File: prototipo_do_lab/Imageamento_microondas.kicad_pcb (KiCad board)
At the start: 2 copper layers, 200 x 150 mm, 89 parts, among them J1 0732511352, J10 0732511352, J11 TB0012-508-03GR, J12 0732511352, J13 0732511352, J2 0732511352, J3 0732511352, J4 0732511352, J5 0732511352, J6 0732511352, J7 0732511352, J8 0732511352, J9 0732511352, U1 SKY13373-460LF, U10 SKY13373-460LF, U11 SKY13373-460LF, U12 SKY13373-460LF, U13 SKY13373-460LF, U14 SKY13373-460LF, U15 SKY13373-460LF, U16 SKY13373-460LF, U17 ESP32-DEVKITC-32E, U18 MCP23016-I_SP, U2 SKY13373-460LF, U3 SKY13373-460LF, U4 SKY13373-460LF, U5 SKY13373-460LF, U6 SKY13373-460LF, U7 SKY13373-460LF, U8 SKY13373-460LF, U9 SKY13373-460LF

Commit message: pin headers added
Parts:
- moved C1 17.3 mm to (128.2, 126.4)
- moved C44 16.3 mm to (178.1, 83.5)
- moved C33 16.3 mm to (172.6, 87.2)
- moved C34 16.3 mm to (176.2, 87.2)
- moved R4 16.3 mm to (172.6, 90.6)
- moved C25 12.1 mm to (101.2, 100.6)
- moved C27 12.1 mm to (95.7, 104.3)
- moved C28 12.1 mm to (99.3, 104.3)
- moved R1 12.1 mm to (95.7, 107.7)
- moved C47 11.1 mm to (210.3, 131.9)
- moved C42 11.1 mm to (208.4, 135.6)
- moved R8 11.1 mm to (204.8, 139.0)
- moved C41 11.1 mm to (204.8, 135.6)
- moved C31 10.9 mm to (66.2, 120.2)
- moved C32 10.9 mm to (69.8, 120.2)
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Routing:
- net /E2_3: track 0.00 -> 84.4 mm
- net (no net): track 84.4 -> 0.00 mm, vias 1 -> 60
- net /CE2_4: vias 0 -> 2
- net /CA_6: vias 0 -> 1
- net /CA_2: vias 0 -> 1

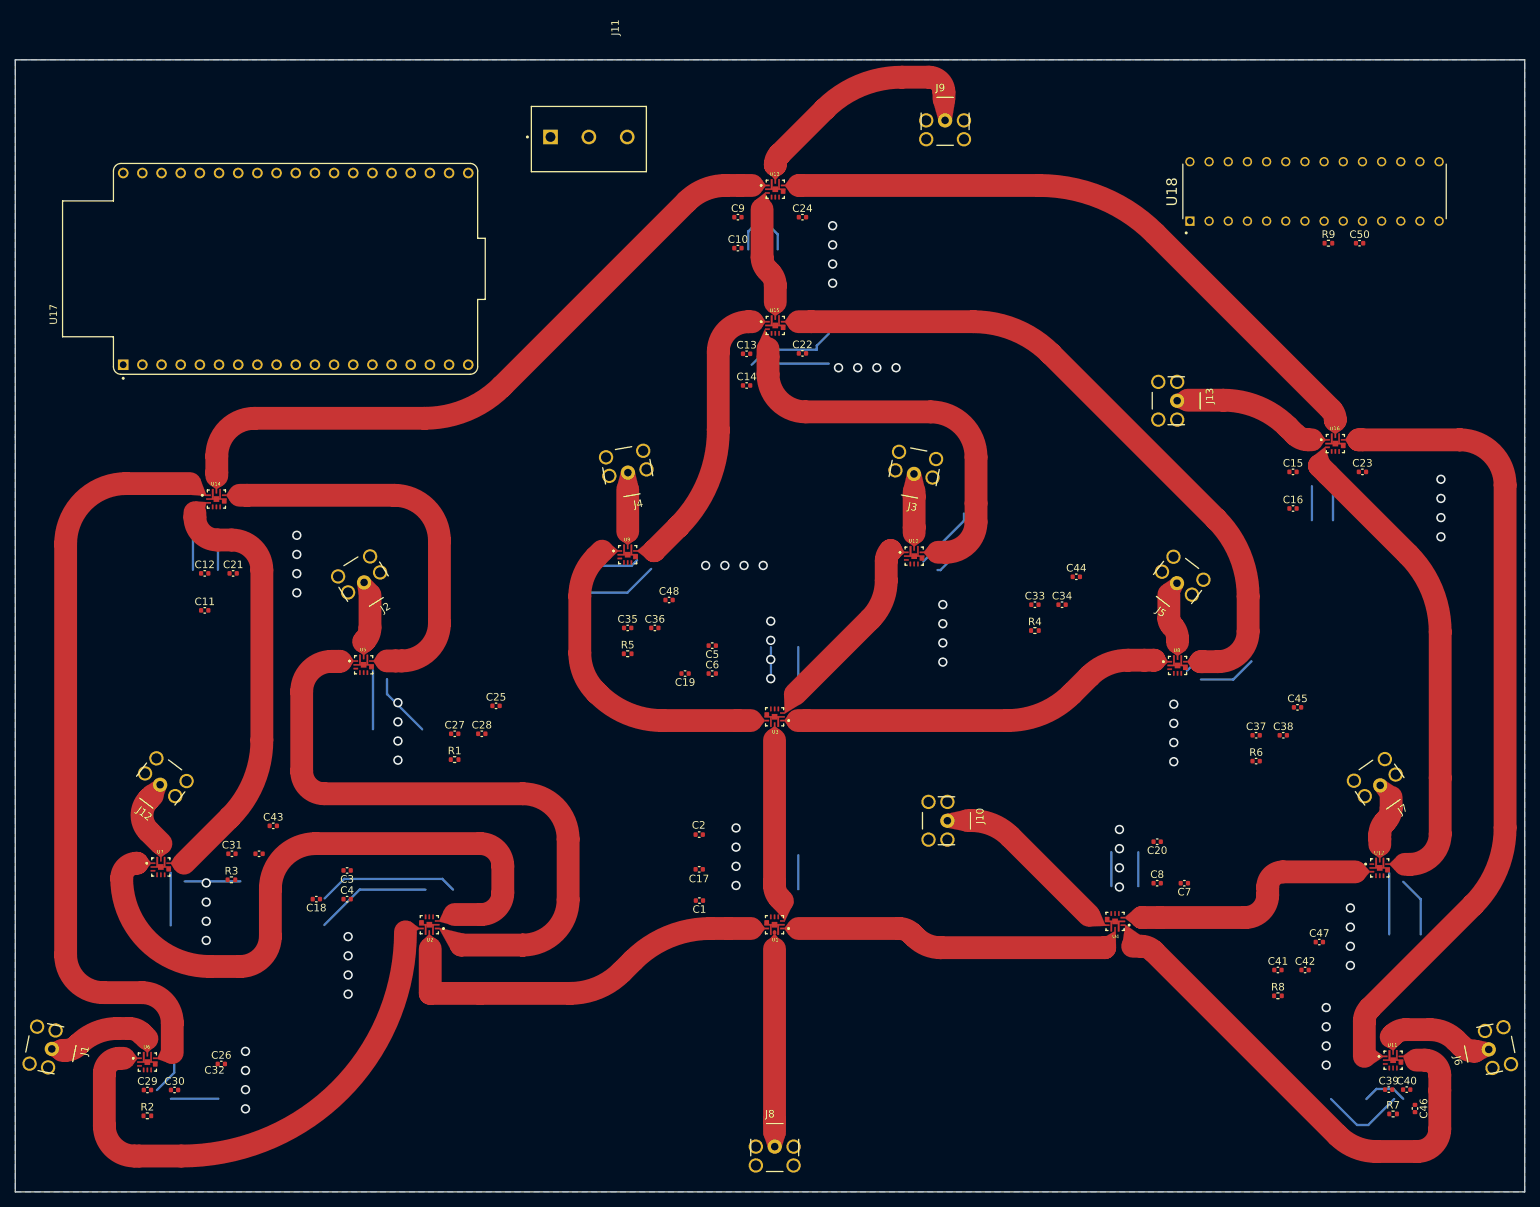
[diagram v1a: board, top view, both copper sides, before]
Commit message: board finished still need validation
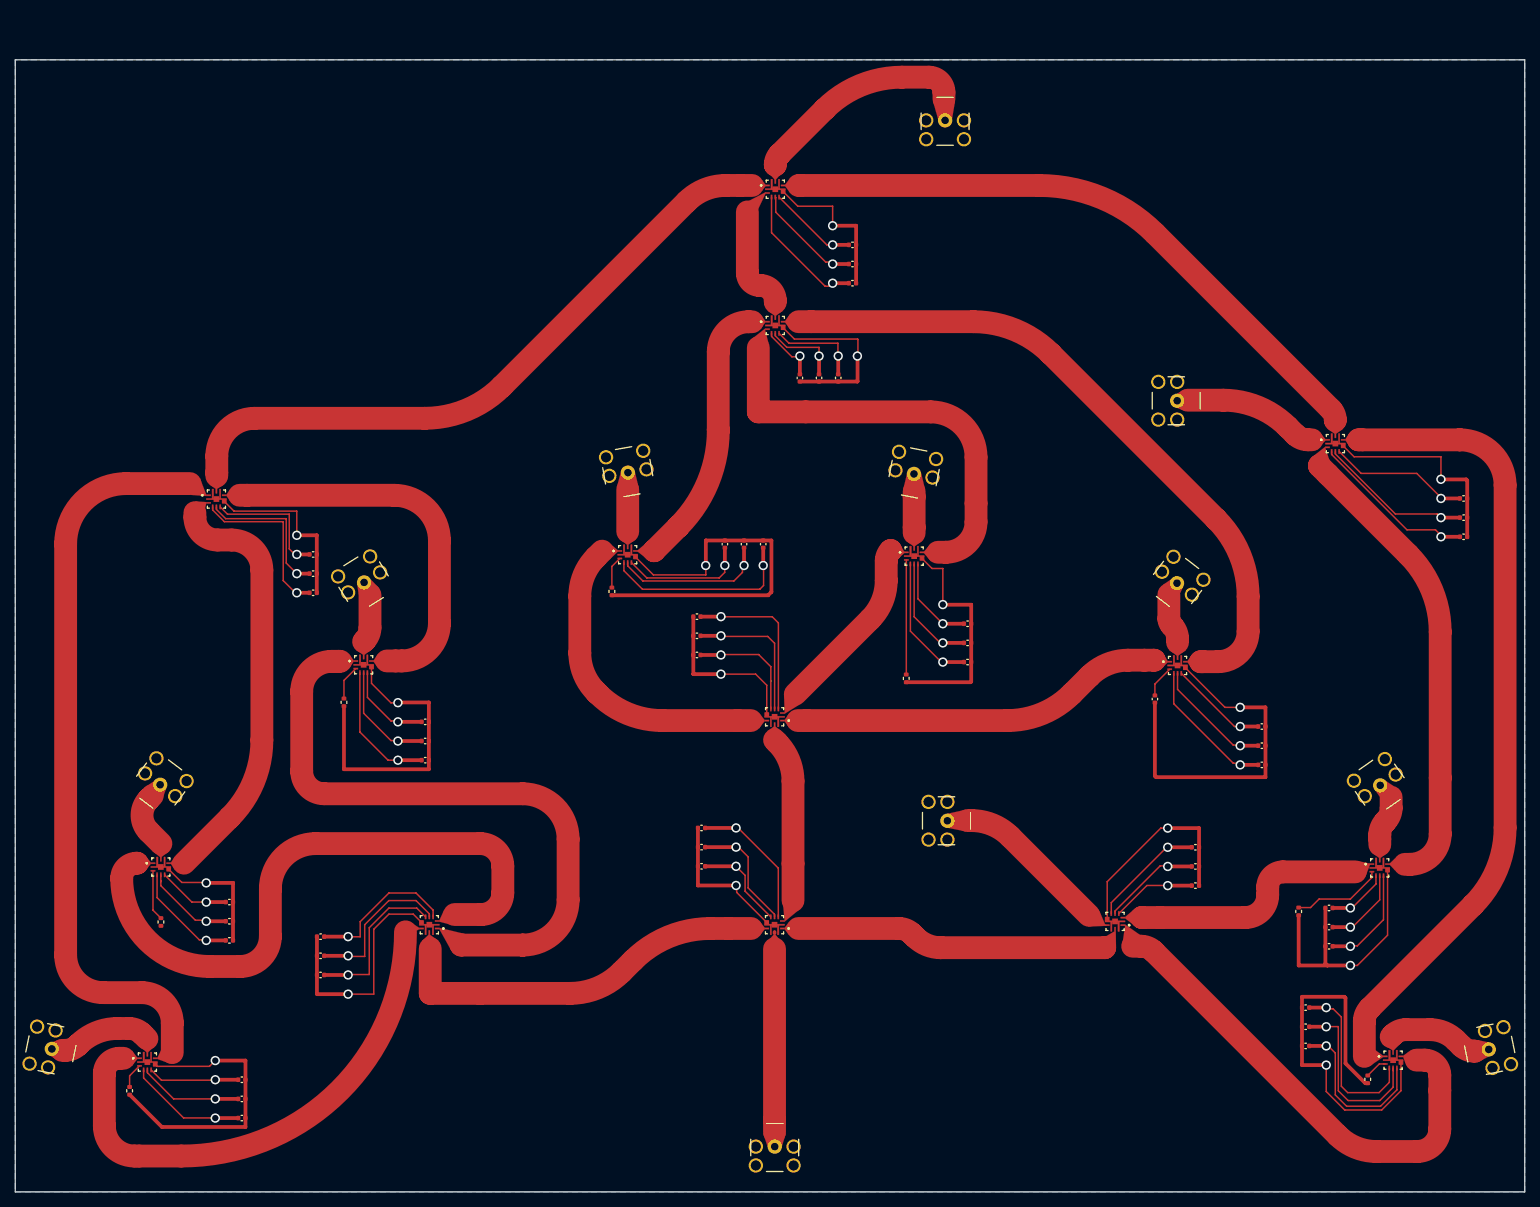
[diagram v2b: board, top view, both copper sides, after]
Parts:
- removed C50: C, Capacitor_SMD:C_0402_1005Metric
- removed J11: TB0012-508-03GR, Conector_alimentacao:SAMESKY_TB0012-508-03GR
- removed R9: R, Resistor_SMD:R_0402_1005Metric
- removed U17: ESP32-DEVKITC-32E, ESP32:MODULE_ESP32-DEVKITC-32E
- removed U18: MCP23016-I_SP, Extensor:DIP787W46P254L3467H508Q28
- moved C15 24.2 mm to (229.4, 78.2), turned to 180 degrees
- moved C16 22.6 mm to (229.4, 75.7)
- moved C35 21.1 mm to (136.6, 79.2), turned to -90 degrees
- moved R4 18.2 mm to (155.6, 97.0), turned to -90 degrees
- moved C9 17.5 mm to (148.4, 44.6), turned to 180 degrees
- moved C46 16.7 mm to (208.5, 145.7), turned to 180 degrees
- moved R1 16.5 mm to (81.0, 100.1), turned to -90 degrees
- moved C36 16.2 mm to (134.1, 79.2), turned to 90 degrees
- moved C40 15.8 mm to (208.5, 143.1), turned to 180 degrees
- moved R6 15.7 mm to (188.5, 99.7), turned to -90 degrees
- moved C44 15.7 mm to (163.7, 89.7)
- moved C39 15.5 mm to (208.5, 140.6)
- moved C10 15.3 mm to (148.4, 42.1)
- moved C11 14.6 mm to (77.0, 85.6), turned to 180 degrees
- moved C12 14.4 mm to (77.0, 83.1)
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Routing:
- net GND: track 0.00 -> 505.4 mm, vias 0 -> 16
- net VDD: track 0.00 -> 236.3 mm, vias 0 -> 16
- net /E2_8: track 0.00 -> 32.0 mm
- net Net-(U12-J3): track 32.0 -> 12.1 mm
- net /CA_9: track 7.85 -> 25.8 mm, vias 0 -> 1
- net /CR2_1: track 4.52 -> 22.4 mm, vias 0 -> 1
- net /CA_14: track 5.99 -> 23.8 mm, vias 0 -> 1
- net /CE2_3: track 4.49 -> 22.1 mm, vias 0 -> 1
- net /CR2_5: track 4.50 -> 22.0 mm, vias 0 -> 1
- net /CR2_6: track 4.70 -> 20.3 mm, vias 0 -> 1
- net Net-(U10-J3): track 0.00 -> 15.2 mm
- net /CR1_1: track 3.03 -> 18.1 mm, vias 0 -> 1
- net /CR2_2: track 4.76 -> 19.6 mm, vias 0 -> 1
- net /CE2_4: track 4.50 -> 18.9 mm, vias 2 -> 1
- net /CE1_1: track 4.50 -> 18.4 mm, vias 0 -> 1
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- added copper zone on B.Cu, net GND
- removed copper zone on B.Cu, net VDD
